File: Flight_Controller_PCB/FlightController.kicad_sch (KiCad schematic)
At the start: 138 parts, among them J1 USB_C_Receptacle_USB2.0_16P, J2 Conn_01x04_Pin, J3 Conn_01x02_Pin, J4 USB_C_Receptacle_USB2.0_16P, J5 Conn_02x09_Top_Bottom, J6 Conn_01x04, J7 Conn_01x02, J8 Micro_SD_Card, Q1 CSD18534Q5A, Q2 CSD18534Q5A, Q3 CSD17308Q3, Q4 CSD17308Q3, Q5 CSD17308Q3, SW1 SW_Push, SW2 BOOT, U1 AP3211K, U10 TPS629203, U11 AMS1117-1.8, U2 ESP32-S3-WROOM-1U-N4R8, U3 CH224K, U4 BQ25798, U6 BQ7791500PWR, U7 LSM6DSOXTR, U8 MPL3115A2ST1, U9 PCF8574P, Y1 ABS06-107-32.768KHZ-T

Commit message: Finished building BQ25798 library, compile successful
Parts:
- removed C12: 2.2uF, symbol Device:C
- removed C60: 10uF, symbol Device:C
- removed D1: 10BQ030, symbol Device:D_Schottky
- removed D3: 1N4745A, Diode_THT:D_DO-41_SOD81_P10.16mm_Horizontal, symbol Diode:1N47xxA
- removed D4: 1N4001, Diode_THT:D_DO-41_SOD81_P10.16mm_Horizontal, symbol Diode:1N4001
- removed D5: LESD5D5.0CT1G, LESD5D5.0CT1G:TVS_LESD5D5.0CT1G, symbol LESD5D5.0CT1G:LESD5D5.0CT1G
- removed D9: LED, symbol Device:LED
- removed J1, J4: USB_C_Receptacle_USB2.0_16P, symbol Connector:USB_C_Receptacle_USB2.0_16P
- removed J6: Conn_01x04, symbol Connector_Generic:Conn_01x04
- removed Q1, Q2: CSD18534Q5A, Package_TO_SOT_SMD:TDSON-8-1, symbol Transistor_FET:CSD18534Q5A
- removed Q3, Q4, Q5: CSD17308Q3, Package_TO_SOT_SMD:TDSON-8-1, symbol Transistor_FET:CSD17307Q5A
- removed R13, R14, R36, R37, R47, R48, R49, R50: 10k, symbol Device:R
- removed R32: 1M, symbol Device:R
- removed R4: 2, symbol Device:R
- removed R51: 1k, symbol Device:R
- removed SW1: SW_Push, symbol Switch:SW_Push
- removed SW2: BOOT, symbol Switch:SW_Push
- added C30: 1uF, Capacitor_SMD:C_0603_1608Metric, symbol Device:C
- added C48, C49: 4.7uF, Capacitor_SMD:C_0603_1608Metric, symbol Device:C
- added C50, C51: 0.1uF, Capacitor_SMD:C_0603_1608Metric, symbol Device:C
- added D1, D2, D3: LESD5D5.0CT1G, ExternalFootprints:TVS_LESD5D5.0CT1G, symbol LESD5D5.0CT1G:LESD5D5.0CT1G
- added D5: DFLS240L, Diode_SMD:D_PowerDI-123, symbol Diode:SS24
- added J1, J4: TYPE-C-31-M-12, ExternalFootprints:HRO_TYPE-C-31-M-12, symbol USB_C:TYPE-C-31-M-12
- added J10, J12, J6: Conn_01x08, TestPoint:TestPoint_THTPad_4.0x4.0mm_Drill2.0mm, symbol Connector_Generic:Conn_01x08
- added J11: Conn_01x02, TestPoint:TestPoint_THTPad_4.0x4.0mm_Drill2.0mm, symbol Connector_Generic:Conn_01x02
- added Q1, Q2, Q3, Q4, Q5: CSD17578Q5A, Package_SON:VSON-8_3.3x3.3mm_P0.65mm_NexFET, symbol Transistor_FET:CSD17581Q3A
- added Q6, Q7: Q_NPN, Package_TO_SOT_SMD:SOT-23, symbol Transistor_BJT:Q_NPN_BCE
- added R53, R58, R59: 10k, Resistor_SMD:R_0402_1005Metric, symbol Device:R
- added R54: 0, Resistor_SMD:R_0603_1608Metric, symbol Device:R
- added R55: 22.1k, Resistor_SMD:R_0402_1005Metric, symbol Device:R
- added R56: 47.5k, Resistor_SMD:R_0402_1005Metric, symbol Device:R
- added R57: 1k, Resistor_SMD:R_0402_1005Metric, symbol Device:R
- added U12: TCA9534, Package_SO:TSSOP-16-1EP_4.4x5mm_P0.65mm, symbol Interface_Expansion:TCA9534
- added U5: CP2102N-Axx-xQFN28, Package_DFN_QFN:QFN-28-1EP_5x5mm_P0.5mm_EP3.35x3.35mm, symbol Interface_USB:CP2102N-Axx-xQFN28
- C1, C10, C11, C13, C14, C15, C16, C17, C18, C19, C20, C21, C22, C23, C24, C25, C26, C27, C28, C33, C34, C35, C36, C37, C38, C39, C4, C40, C41, C42, C43, C44, C45, C46, C47, C5, C6, C7, C8, C9: footprint (none) -> Capacitor_SMD:C_0603_1608Metric
- C2: footprint (none) -> Capacitor_SMD:C_1206_3216Metric
- C3: footprint (none) -> Capacitor_SMD:C_0805_2012Metric
- C31: renamed from C63; footprint (none) -> Capacitor_SMD:C_0603_1608Metric
- C32: renamed from C64; footprint (none) -> Capacitor_SMD:C_0603_1608Metric
- D6, D7, D8: footprint (none) -> LED_SMD:LED_0402_1005Metric
- J2: footprint (none) -> Connector_JST:JST_XH_B4B-XH-A_1x04_P2.50mm_Vertical
- J3: footprint (none) -> Connector_AMASS:AMASS_XT60-M_1x02_P7.20mm_Vertical
- J5: footprint (none) -> TestPoint:TestPoint_THTPad_2.0x2.0mm_Drill1.0mm
- J7: footprint (none) -> TestPoint:TestPoint_THTPad_4.0x4.0mm_Drill2.0mm
- J8: footprint (none) -> Connector_Card:microSD_HC_Molex_104031-0811
- L1: footprint (none) -> Inductor_SMD:L_0603_1608Metric
- L2: renamed from L4; footprint (none) -> Inductor_SMD:L_Coilcraft_XAL7020-222
- L3: footprint (none) -> Inductor_SMD:L_Coilcraft_LPS4018
- R1, R10, R11, R12, R15, R16, R17, R18, R19, R2, R20, R21, R22, R23, R24, R25, R26, R28, R29, R3, R30, R31, R33, R34, R35, R38, R39, R41, R44, R45, R46, R5, R52, R6, R7, R8, R9: footprint (none) -> Resistor_SMD:R_0402_1005Metric
- R27: value 3.3M -> 1M; footprint (none) -> Resistor_SMD:R_0402_1005Metric
- R42, R43: value 22 -> 10k; footprint (none) -> Resistor_SMD:R_0402_1005Metric
- TH1, TH2: footprint (none) -> Resistor_SMD:R_0805_2012Metric
- TP1, TP2: footprint (none) -> TestPoint:TestPoint_THTPad_1.5x1.5mm_Drill0.7mm
- U2: footprint ESP32-S3-WROOM-1U-N4R8:XCVR_ESP32-S3-WROOM-1U-N4R8 -> ExternalFootprints:XCVR_ESP32-S3-WROOM-1U-N4R8
- U6: footprint PW24_TEX -> ExternalFootprints:PW24_TEX
- U7: footprint LSM6DSOXTR:PQFN50P250X300X86-14N -> ExternalFootprints:PQFN50P250X300X86-14N
- U9: value PCF8574P -> TCA9534; footprint Package_DIP:DIP-16_W7.62mm -> Package_SO:TSSOP-16-1EP_4.4x5mm_P0.65mm; symbol Interface_Expansion:PCF8574P -> Interface_Expansion:TCA9534
- Y1: footprint ABS06-107-32.768KHZ-T:XTAL_ABS06-107-32.768KHZ-T -> ExternalFootprints:XTAL_ABS06-107-32.768KHZ-T
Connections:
- net +V_BAT is gone; now on net +VBAT: J7.1 (Pin_1)
- net +1V8: now also C43.1, C44.1
- net +3V3: now also R42.2, R43.2, C48.1, C49.1, C50.1, C51.1, J11.1 (Pin_1), R53.2, R57.1, U12.1 (A0), U12.16 (VDD), U5.6 (VDD), U5.7 (VREGIN); no longer C43.1, C44.1
- net BAT_2: now also Q5.1 (S), Q5.2 (S), Q5.3 (S)
- net BAT_3: now also Q4.1 (S), Q4.2 (S), Q4.3 (S)
- net BAT_GND: now also Q3.1 (S), Q3.2 (S), Q3.3 (S)
- net BOOT_MODE: now also U2.27 (IO0), Q7.2 (C); no longer U2.16 (IO46)
- net BQ_SCL: now also R43.1, U2.17 (IO9), U12.14 (SCL); no longer U2.28 (IO35)
- net BQ_SDA: now also R42.1, U2.12 (IO8), R54.2; no longer U2.23 (IO21), U7.14 (SDA)
- net CC1: now also J4.A5 (CC1)
- net CC2: now also J4.B5 (CC2)
- net EN: now also Q6.2 (C)
- net GND: now also J5.8 (Pin_8), J8.10 (GND), J8.9 (GND), R19.1, R21.1, R27.1, TH1.2, U10.9 (GND), U2.41 (GND), U6.20 (CCFG), U6.23 (CTRC), U6.24 (CTRD), U9.17 (GND), C30.1, C48.2, C49.2, C50.2, C51.2, D1.2, D2.2, D3.2, D5.2 (A), J1.A1_B12 (GND), J1.B1_A12 (GND), J1.S1 (SHIELD), J1.S2 (SHIELD), J1.S3 (SHIELD), J1.S4 (SHIELD), J11.2 (Pin_2), J4.A1_B12 (GND), J4.B1_A12 (GND), J4.S1 (SHIELD), J4.S2 (SHIELD), J4.S3 (SHIELD), J4.S4 (SHIELD), J6.8 (Pin_8), Q2.5 (D), R56.2, U12.17 (VDD), U12.2 (A1), U12.3 (A2), U12.8 (GND), U5.11 (~{SUSPEND}), U5.29 (GND), U5.3 (GND)
- net IMU_INT1: now also U2.34 (IO41); no longer U2.21 (IO13)
- net IMU_INT2: now also U2.35 (IO42); no longer U2.22 (IO14)
- net MOTOR_PWM_1: now also J6.5 (Pin_5), U12.9 (P4)
- net MOTOR_PWM_2: now also J6.6 (Pin_6), U12.10 (P5)
- net MOTOR_PWM_3: now also J6.7 (Pin_7), U12.11 (P6)
- net REGN: now also C15.1, U4.5 (REGN)
- net SD_CS: now also U2.18 (IO10)
- net SD_MISO: now also U2.21 (IO13)
- net SD_MOSI: now also U2.19 (IO11)
- net SD_SCLK: now also U2.20 (IO12)
- net USB_D+: now also D1.1, J1.A6 (DP1), J1.B6 (DP2), U5.4 (D+); no longer R43.1
- net USB_D-: now also D2.1, J1.A7 (DN1), J1.B7 (DN2), U5.5 (D-); no longer R42.1
- net USB_D_BAT+: now also J4.A6 (DP1), J4.B6 (DP2)
- net USB_D_BAT-: now also J4.A7 (DN1), J4.B7 (DN2)
- net VC0: now also Q3.4 (G)
- net VC1: now also Q4.4 (G)
- net VC2: now also Q5.4 (G)
- net at R28.1, R29.1, R30.1: now also Q1.1 (S), Q1.2 (S), Q1.3 (S)
- net at R25.1, R28.2: now also Q1.4 (G)
- net at R33.1: now also Q5.5 (D)
- net at R26.1, R27.2: now also Q2.4 (G)
- net at U2.13 (IO19): no longer R42.2
- net at R2.1: now also J1.A5 (CC1)
- net at R34.1: now also Q4.5 (D)
- net at R35.1: now also Q3.5 (D)
- net at U2.14 (IO20): no longer R43.2
- net at R1.1: now also J1.B5 (CC2)
- net at C40.2, L3.1, U1.6 (SW): now also D5.1 (K)
- net IO17: now reaches U2.10 (IO17)
- net IO17: now also J12.7 (Pin_7)
- net IO18: now reaches U2.11 (IO18)
- net IO18: now also J12.8 (Pin_8)
- net IO3: now reaches U2.15 (IO3)
- net IO3: now also J10.8 (Pin_8)
- net IO47: now reaches U2.24 (IO47)
- net IO47: now also J10.5 (Pin_5)
- net IO48: now reaches U2.25 (IO48)
- net IO48: now also J10.4 (Pin_4)
- net IO36: now reaches U2.29 (IO36)
- net IO36: now also J10.2 (Pin_2)
- net IO37: now reaches U2.30 (IO37)
- net IO37: now also J10.1 (Pin_1)
- net CAM_AVAILABLE_PC: now reaches U2.31 (IO38)
- net CAM_AVAILABLE_PC: now also J5.4 (Pin_4)
- net CAM_FRAME_VS: now reaches U2.32 (IO39)
- net CAM_FRAME_VS: now also J5.5 (Pin_5)
- net CAM_ROW_HS: now reaches U2.33 (IO40)
- net CAM_ROW_HS: now also J5.6 (Pin_6)
- net RXD: now reaches U2.36 (RXD0)
- net RXD: now also U5.26 (TXD)
- net TXD: now reaches U2.37 (TXD0)
- net TXD: now also U5.25 (RXD)
- net IO2: now reaches U2.38 (IO2)
- net IO2: now also J12.2 (Pin_2)
- net IO1: now reaches U2.39 (IO1)
- net IO1: now also J12.1 (Pin_1)
- net IO4: now reaches U2.4 (IO4)
- net IO4: now also J12.3 (Pin_3)
- net IO5: now reaches U2.5 (IO5)
- net IO5: now also J12.4 (Pin_4)
- net IO6: now reaches U2.6 (IO6)
- net IO6: now also J12.5 (Pin_5)
- net IO7: now reaches U2.7 (IO7)
- net IO7: now also J12.6 (Pin_6)
- net +BAT_VBUS renamed VBUS
- net VBUS: now also D3.1, J1.A4_B9 (VBUS), J1.B4_A9 (VBUS), J4.A4_B9 (VBUS), J4.B4_A9 (VBUS), R55.1
- removed net CAM_AVAILABLE: J5.4 (Pin_4), U2.18 (IO10)
- removed net CAM_FRAME: J5.5 (Pin_5), U2.19 (IO11)
- removed net CAM_ROW: J5.6 (Pin_6), U2.20 (IO12)
- net GPIO45: no longer names the net of U2.26 (IO45)
- new net: R53.1, U12.13 (~{INT})
- new net: Q1.5 (D), Q2.1 (S), Q2.2 (S), Q2.3 (S)
- new net: Q6.1 (B), R58.2
- new net: Q7.1 (B), R59.2
- new net: R57.2, U5.9 (~{RST})
- new net CP2102N_GPIO0: U5.19 (~{TXT}/GPIO.0)
- new net CP2102N_GPIO1: U5.18 (~{RXT}/GPIO.1)
- new net CP2102N_GPIO2: U5.17 (RS485/GPIO.2)
- new net CP2102N_GPIO3: U5.16 (~{WAKEUP}/GPIO.3)
- new net CP2102N_GPIO4: U5.22 (GPIO.4)
- new net CP2102N_GPIO5: U5.21 (GPIO.5)
- new net CP2102N_GPIO6: U5.20 (GPIO.6)
- new net DTR: Q7.3 (E), R58.1, U5.28 (~{DTR})
- new net IMU_SDA: R54.1, U12.15 (SDA), U7.14 (SDA)
- new net IO14: J10.7 (Pin_7), U2.22 (IO14)
- new net IO21: J10.6 (Pin_6), U2.23 (IO21)
- new net IO35: J10.3 (Pin_3), U2.28 (IO35)
- new net MISC: J6.4 (Pin_4), U12.7 (P3)
- new net RTS: Q6.3 (E), R59.1, U5.24 (~{RTS})
- new net SERVO_1: J6.1 (Pin_1), U12.4 (P0)
- new net SERVO_2: J6.2 (Pin_2), U12.5 (P1)
- new net SERVO_3: J6.3 (Pin_3), U12.6 (P2)
- new net USB_DATA_VBUS: C30.2, R55.2, R56.1, U5.8 (VBUS)
- now unconnected: U6.16 (CBI)
- no-connect marks 16 -> 35
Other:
- moved on the sheet: C15, C31, C32, C4, C43, C44, D6, D7, D8, J7, R1, R2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

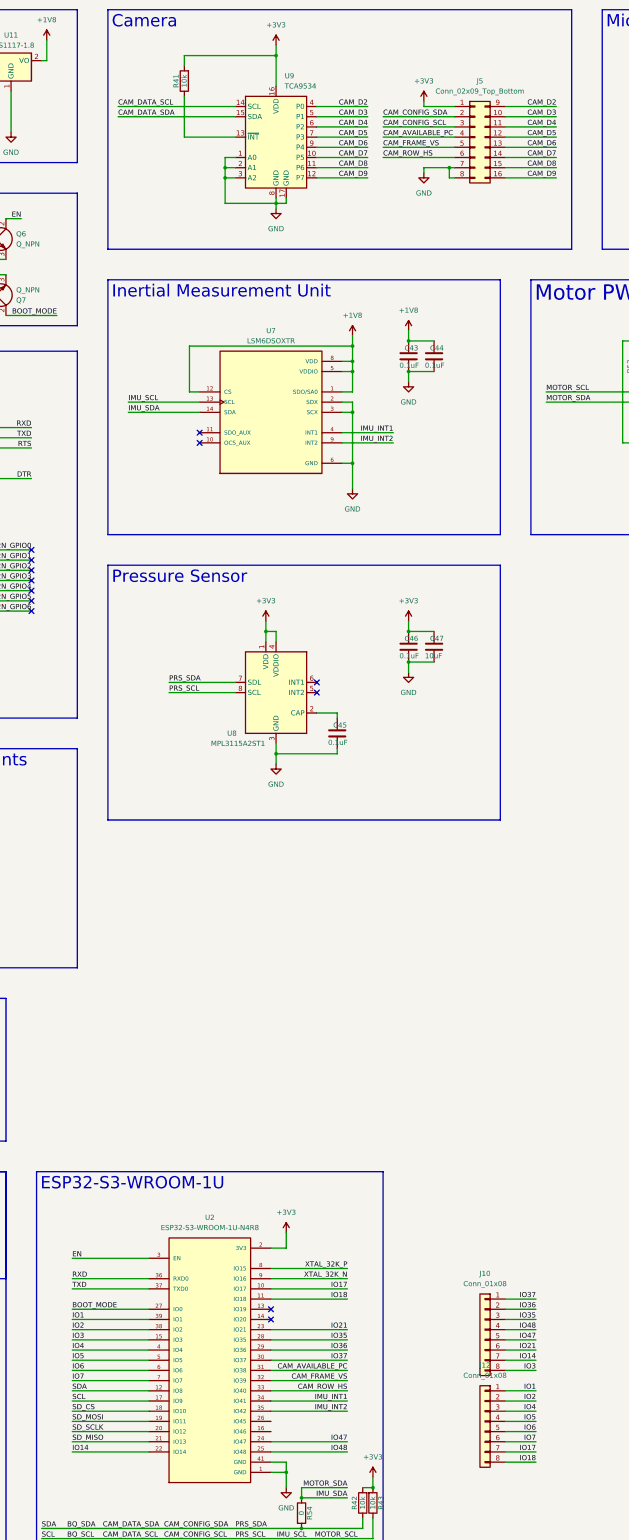
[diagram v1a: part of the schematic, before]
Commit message: OV5640 configuration completed, build successful
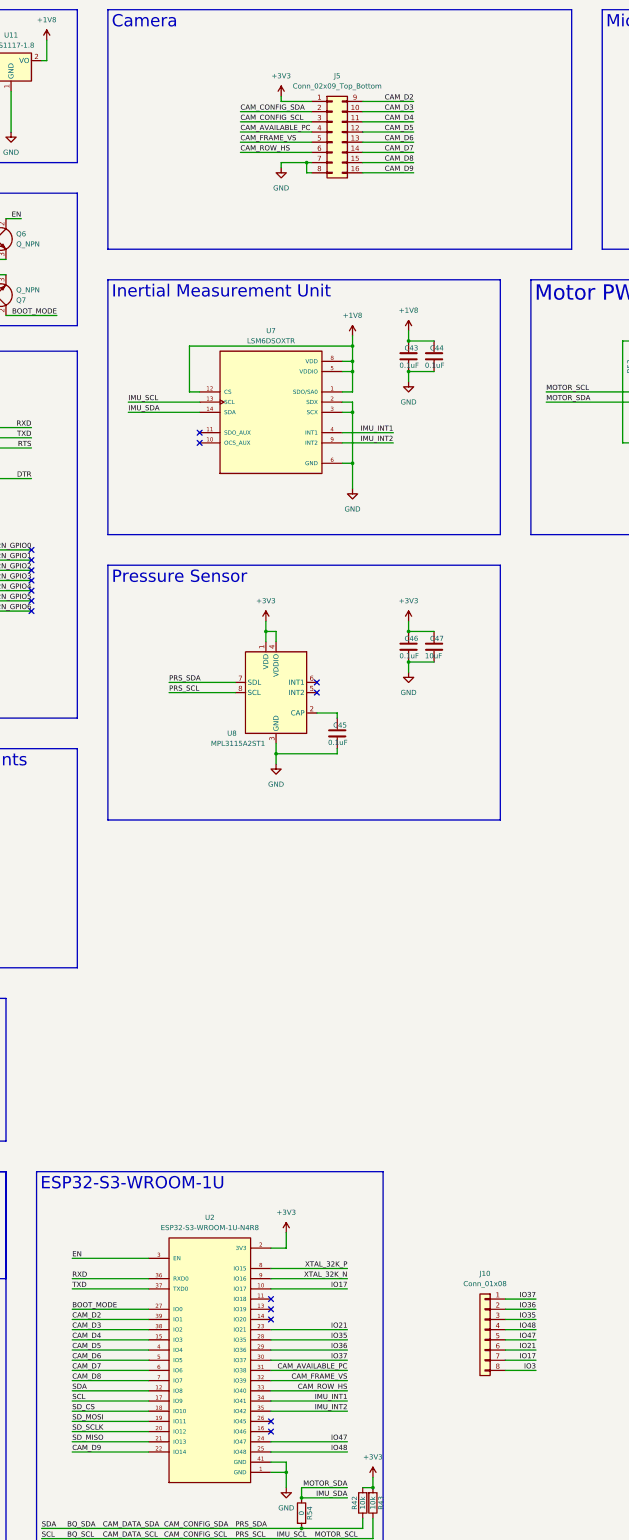
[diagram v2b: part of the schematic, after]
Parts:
- removed J12: Conn_01x08, TestPoint:TestPoint_THTPad_4.0x4.0mm_Drill2.0mm, symbol Connector_Generic:Conn_01x08
- removed R41: 10k, Resistor_SMD:R_0402_1005Metric, symbol Device:R
- removed U9: TCA9534, Package_SO:TSSOP-16-1EP_4.4x5mm_P0.65mm, symbol Interface_Expansion:TCA9534
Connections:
- net IO1 is gone; now on net CAM_D2: U2.39 (IO1)
- net IO2 is gone; now on net CAM_D3: U2.38 (IO2)
- net IO4 is gone; now on net CAM_D5: U2.4 (IO4)
- net IO5 is gone; now on net CAM_D6: U2.5 (IO5)
- net IO6 is gone; now on net CAM_D7: U2.6 (IO6)
- net IO7 is gone; now on net CAM_D8: U2.7 (IO7)
- net CAM_D4: now also U2.15 (IO3)
- net CAM_D9: now also U2.22 (IO14)
- net IO17: now also J10.7 (Pin_7)
- net IO3: no longer U2.15 (IO3)
- removed net IO14: J10.7 (Pin_7), U2.22 (IO14)
- net IO18: no longer names the net of U2.11 (IO18)
- no-connect marks 35 -> 38
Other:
- moved on the sheet: J5

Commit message: Added media, added STEP file of PCB
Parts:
- added R47, R48, R49, R50: 10k, Resistor_SMD:R_0402_1005Metric, symbol Device:R
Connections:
- net +1V8: now also R49.2, R50.2
- net +3V3: now also J10.1 (Pin_1), R47.2, R48.2
- net IMU_INT1: now also R49.1
- net IMU_INT2: now also R50.1
- net PRS_INT2: now reaches U8.5 (INT2)
- net PRS_INT2: now also U2.29 (IO36), R48.1
- net PRS_INT1: now reaches U8.6 (INT1)
- net PRS_INT1: now also U2.30 (IO37), R47.1
- net IO18: now reaches U2.11 (IO18)
- net IO18: now also J10.2 (Pin_2)
- removed net IO36: J10.2 (Pin_2), U2.29 (IO36)
- removed net IO37: J10.1 (Pin_1), U2.30 (IO37)
- no-connect marks 38 -> 35

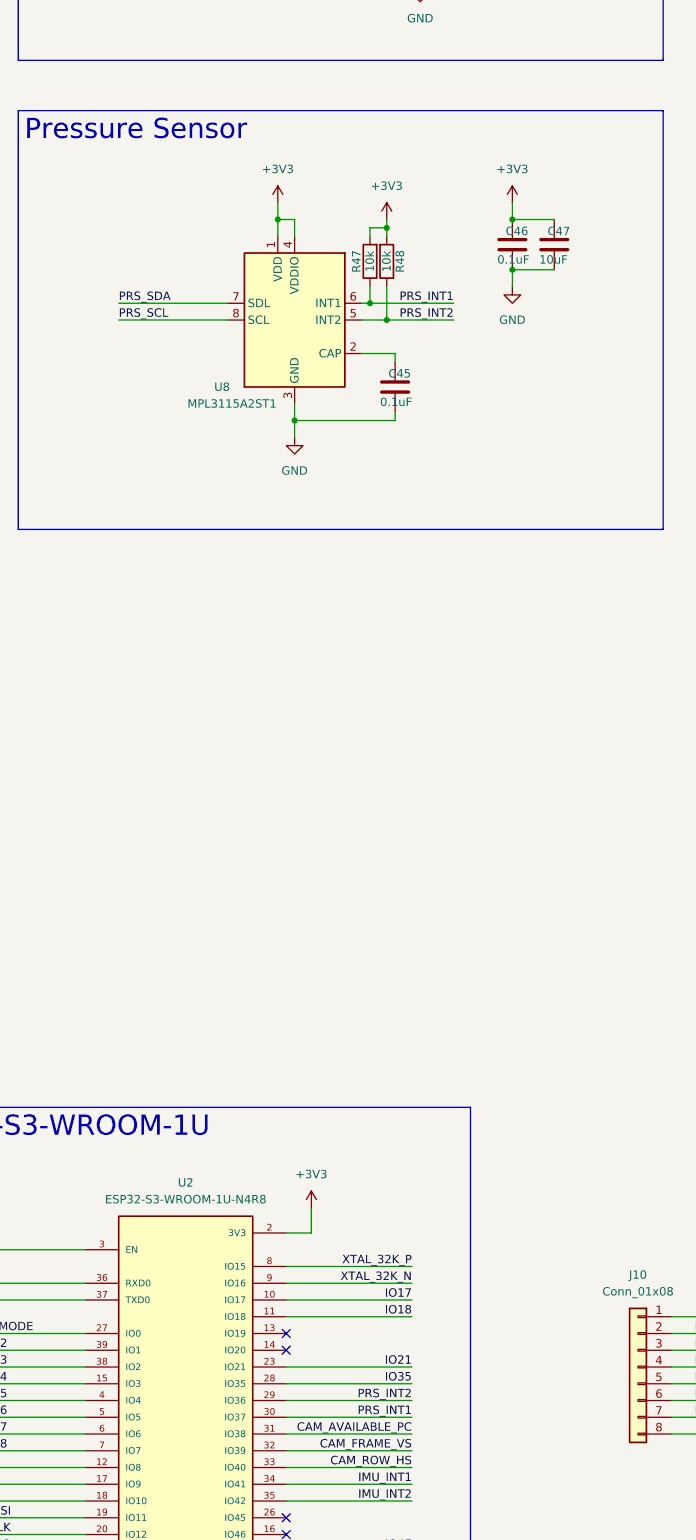
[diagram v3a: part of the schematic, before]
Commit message: Finalize for submission and add BOM
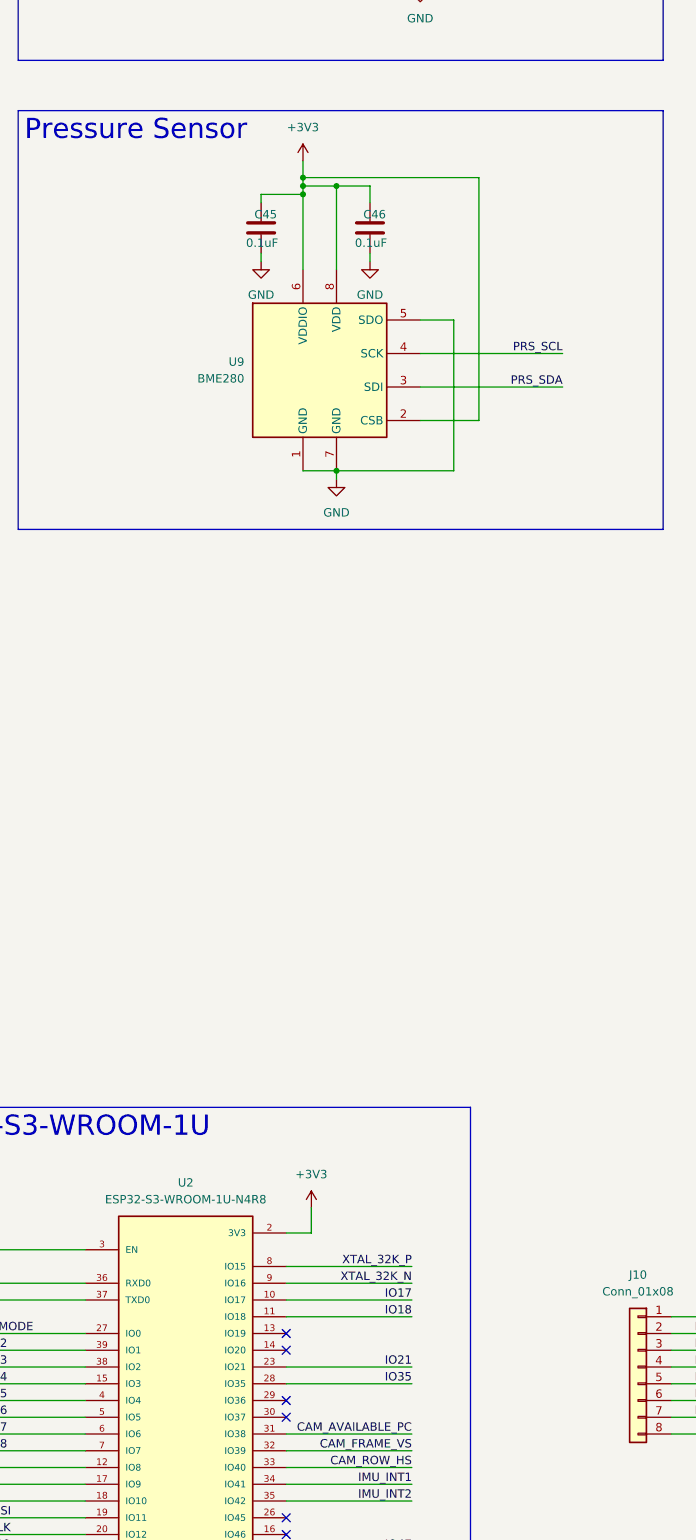
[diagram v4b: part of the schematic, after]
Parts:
- removed C47: 10uF, Capacitor_SMD:C_0603_1608Metric, symbol Device:C
- removed R47, R48: 10k, Resistor_SMD:R_0402_1005Metric, symbol Device:R
- removed U8: MPL3115A2ST1, Package_LGA:NXP_LGA-8_3x5mm_P1.25mm_H1.1mm, symbol Sensor_Pressure:MPL3115A2
- added U9: BME280, Package_LGA:Bosch_LGA-8_2.5x2.5mm_P0.65mm_ClockwisePinNumbering, symbol Sensor:BME280
- L2: footprint Inductor_SMD:L_Coilcraft_XAL7020-222 -> Inductor_SMD:L_1008_2520Metric
- L3: footprint Inductor_SMD:L_Coilcraft_LPS4018 -> Inductor_SMD:L_Abracon_ASPI-4030S
- R33, R34, R35: footprint Resistor_SMD:R_0402_1005Metric -> Resistor_SMD:R_0805_2012Metric_Pad1.20x1.40mm_HandSolder
- U10: footprint Package_SON:WSON-8-1EP_2x2mm_P0.5mm_EP0.9x1.6mm_ThermalVias -> Package_TO_SOT_SMD:SOT-583-8
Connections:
- net +3V3: now also C45.1, U9.2 (CSB), U9.6 (VDDIO), U9.8 (VDD)
- net BQ_SCL: now also U9.4 (SCK)
- net BQ_SDA: now also U9.3 (SDI)
- net GND: now also U9.1 (GND), U9.5 (SDO), U9.7 (GND)
- net PRS_INT1: no longer names the net of U2.30 (IO37)
- net PRS_INT2: no longer names the net of U2.29 (IO36)
- no-connect marks 35 -> 37
